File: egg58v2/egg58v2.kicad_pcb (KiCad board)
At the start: 2 copper layers, 141.1 x 125.8 mm, 37 parts, among them J1 AudioJack4, SW11 SW_PUSH_LED, SW12 SW_PUSH_LED, SW13 SW_PUSH_LED, SW14 SW_PUSH_LED, SW15 SW_PUSH_LED, SW16 SW_PUSH_LED, SW21 SW_PUSH_LED, SW22 SW_PUSH_LED, SW23 SW_PUSH_LED, SW24 SW_PUSH_LED, SW25 SW_PUSH_LED, SW26 SW_PUSH_LED, SW31 SW_PUSH_LED, SW32 SW_PUSH_LED, SW33 SW_PUSH_LED, SW34 SW_PUSH_LED, SW35 SW_PUSH_LED, SW36 SW_PUSH_LED, SW41 SW_PUSH_LED, SW42 SW_PUSH_LED, SW43 SW_PUSH_LED, SW44 SW_PUSH_LED, SW45 SW_PUSH_LED, SW46 SW_PUSH_LED, SW52 SW_PUSH_LED, SW53 SW_PUSH_LED, SW54 SW_PUSH_LED, SW55 SW_PUSH_LED, SW56 SW_PUSH_LED, U1 Elite-C

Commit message: columns
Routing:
- net Col6: track 70.7 -> 193.5 mm
- net Col5: track 88.7 -> 204.7 mm
- net Col2: track 140.3 -> 234.0 mm
- net Col3: track 124.5 -> 217.9 mm
- net Col4: track 107.5 -> 200.9 mm
- net Col1: track 162.1 -> 234.3 mm

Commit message: underp footprints and route everything i guess
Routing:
- net GND: track 5.95 -> 224.4 mm, vias 0 -> 57
- net VCC: track 724.2 -> 908.1 mm, vias 6 -> 35
- net Net-(SW46-Pad2): track 0.00 -> 69.0 mm, vias 0 -> 2
- net Col4: track 200.9 -> 249.1 mm, vias 2 -> 7
- net Col5: track 204.7 -> 252.9 mm, vias 2 -> 7
- net Net-(SW55-Pad4): track 0.00 -> 46.6 mm, vias 0 -> 2
- net Col2: track 234.0 -> 280.0 mm, vias 2 -> 7
- net Col3: track 217.9 -> 263.3 mm, vias 2 -> 7
- net Net-(SW54-Pad4): track 0.00 -> 44.6 mm, vias 0 -> 2
- net Net-(SW11-Pad2): track 0.00 -> 43.5 mm, vias 0 -> 3
- net Col6: track 193.5 -> 236.4 mm, vias 0 -> 5
- net Col1: track 234.3 -> 274.7 mm, vias 2 -> 6
- net Net-(SW31-Pad2): track 0.00 -> 39.8 mm, vias 0 -> 2
- net Net-(SW41-Pad2): track 0.00 -> 36.7 mm, vias 0 -> 4
- net Net-(SW26-Pad2): track 0.00 -> 33.4 mm, vias 0 -> 2
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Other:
- board size 141.1 x 125.8 mm -> 141.1 x 127.1 mm

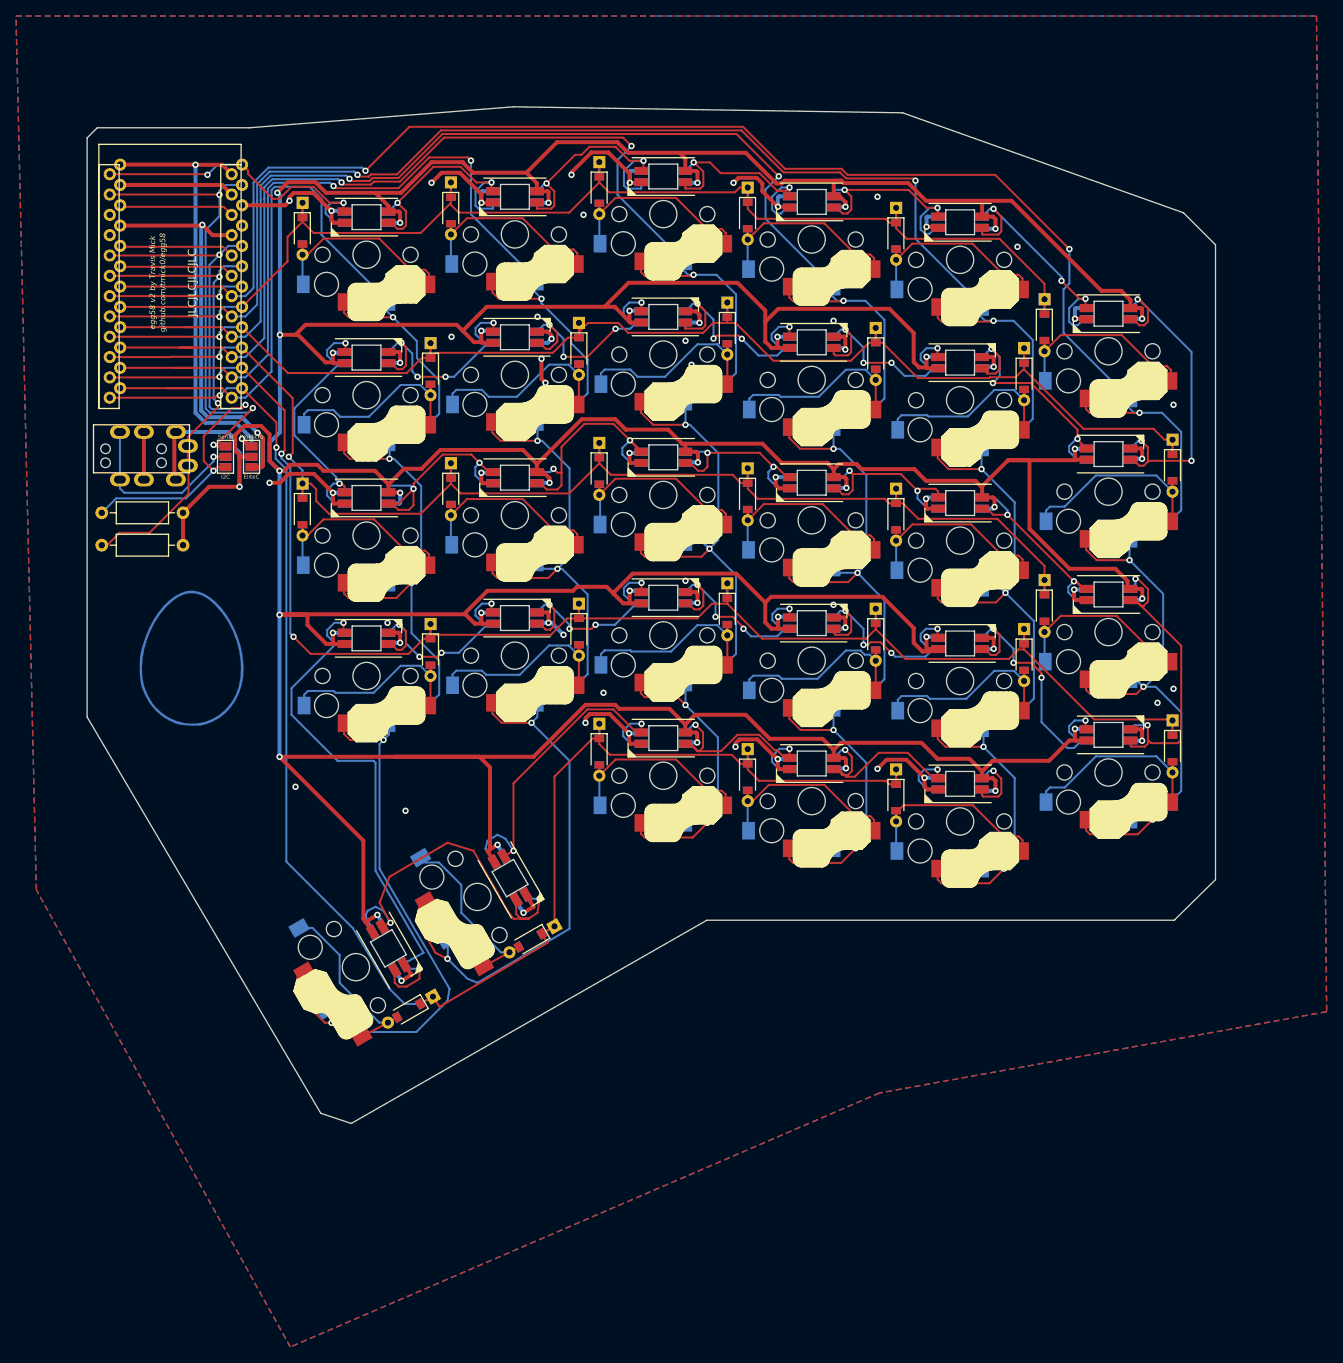
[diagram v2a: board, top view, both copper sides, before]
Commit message: fix (most) vias through silks
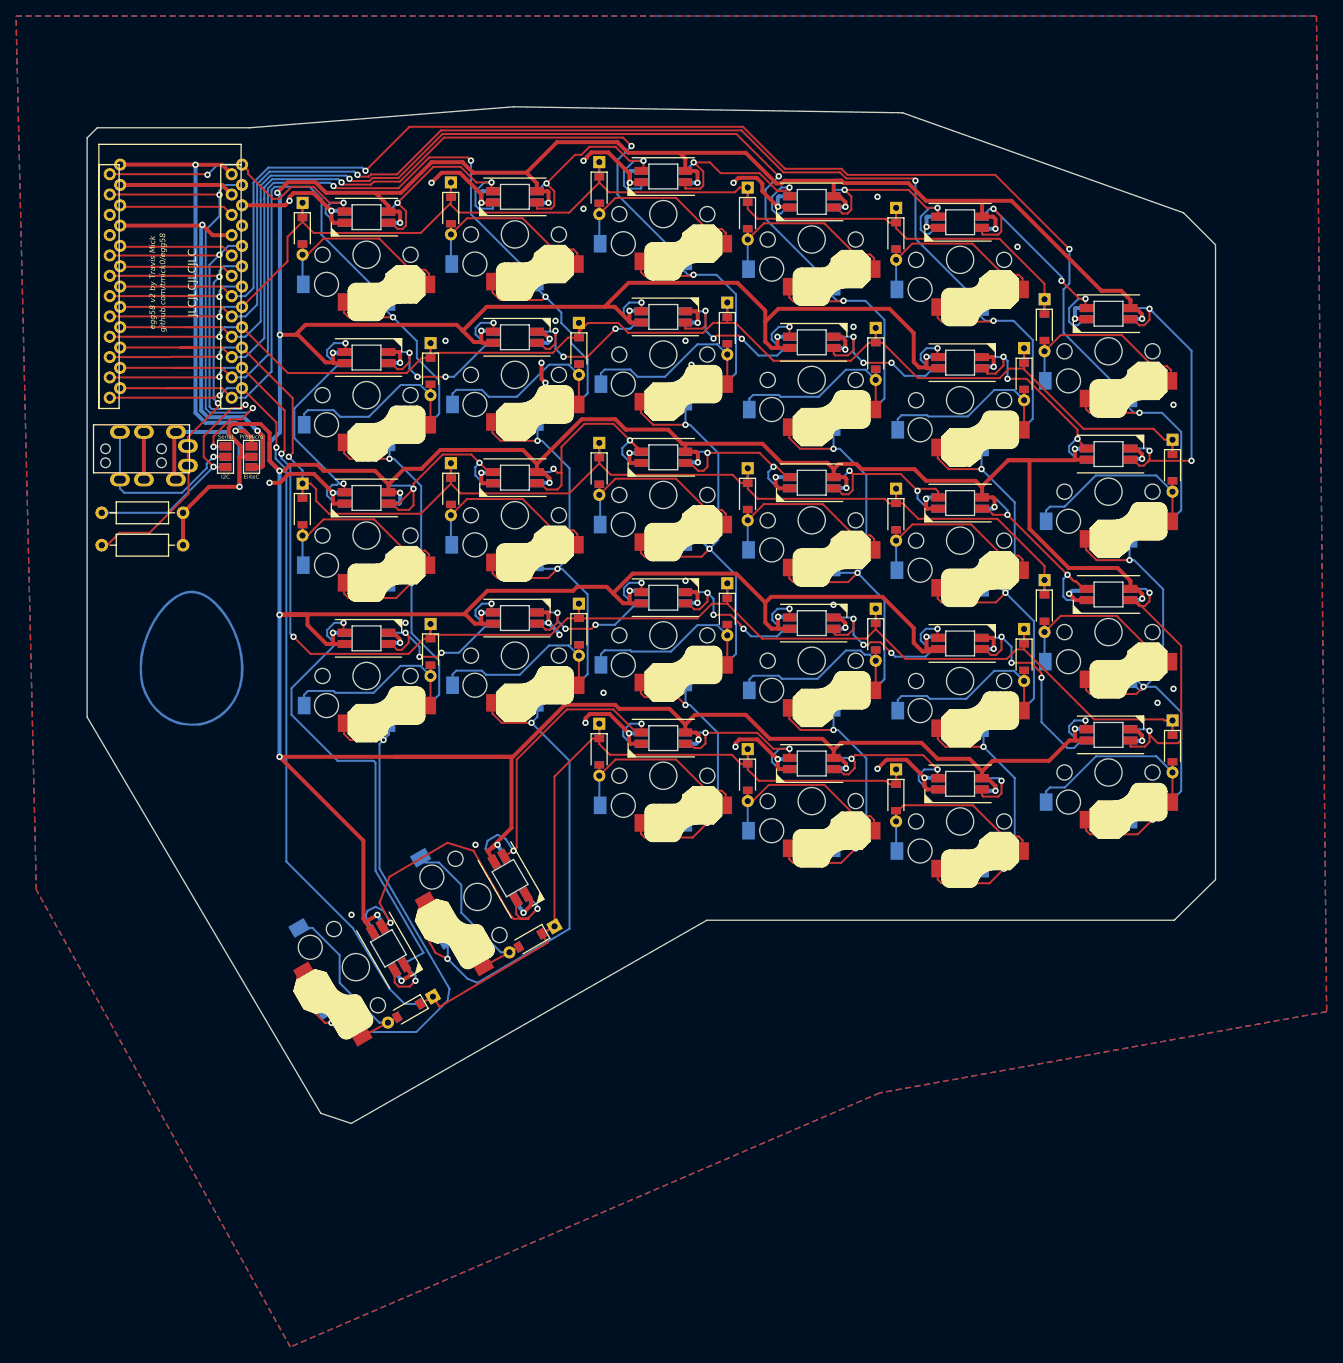
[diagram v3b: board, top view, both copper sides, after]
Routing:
- net GND: track 224.4 -> 218.7 mm
- net VCC: track 908.1 -> 913.4 mm
- net Net-(SW52-Pad4): track 30.3 -> 25.9 mm
- net Net-(SW53-Pad4): track 28.8 -> 24.5 mm
- net Net-(SW21-Pad2): track 32.8 -> 29.0 mm
- net Net-(SW11-Pad2): track 43.5 -> 40.1 mm
- net VBUS: track 57.9 -> 60.5 mm
- net Net-(SW31-Pad4): track 26.7 -> 29.2 mm
- net Net-(SW22-Pad2): track 30.6 -> 28.0 mm
- net Net-(SW25-Pad2): track 30.5 -> 28.1 mm
- net Net-(SW45-Pad2): track 29.4 -> 27.5 mm
- net Net-(SW23-Pad2): track 31.3 -> 29.3 mm
- net Net-(SW41-Pad2): track 36.7 -> 34.8 mm
- net Net-(SW42-Pad2): track 29.7 -> 27.9 mm
- net Net-(SW24-Pad2): track 30.4 -> 28.6 mm
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
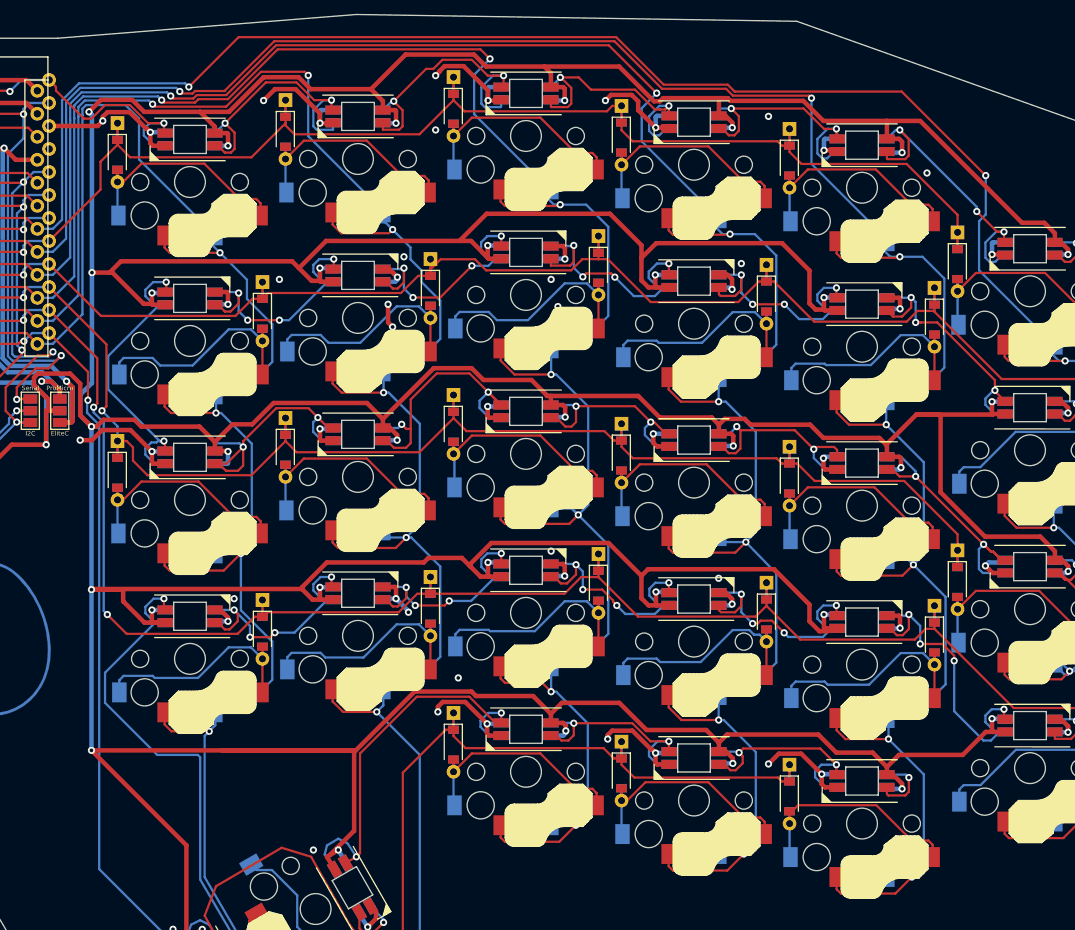
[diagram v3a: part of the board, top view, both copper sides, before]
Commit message: Mounting holes
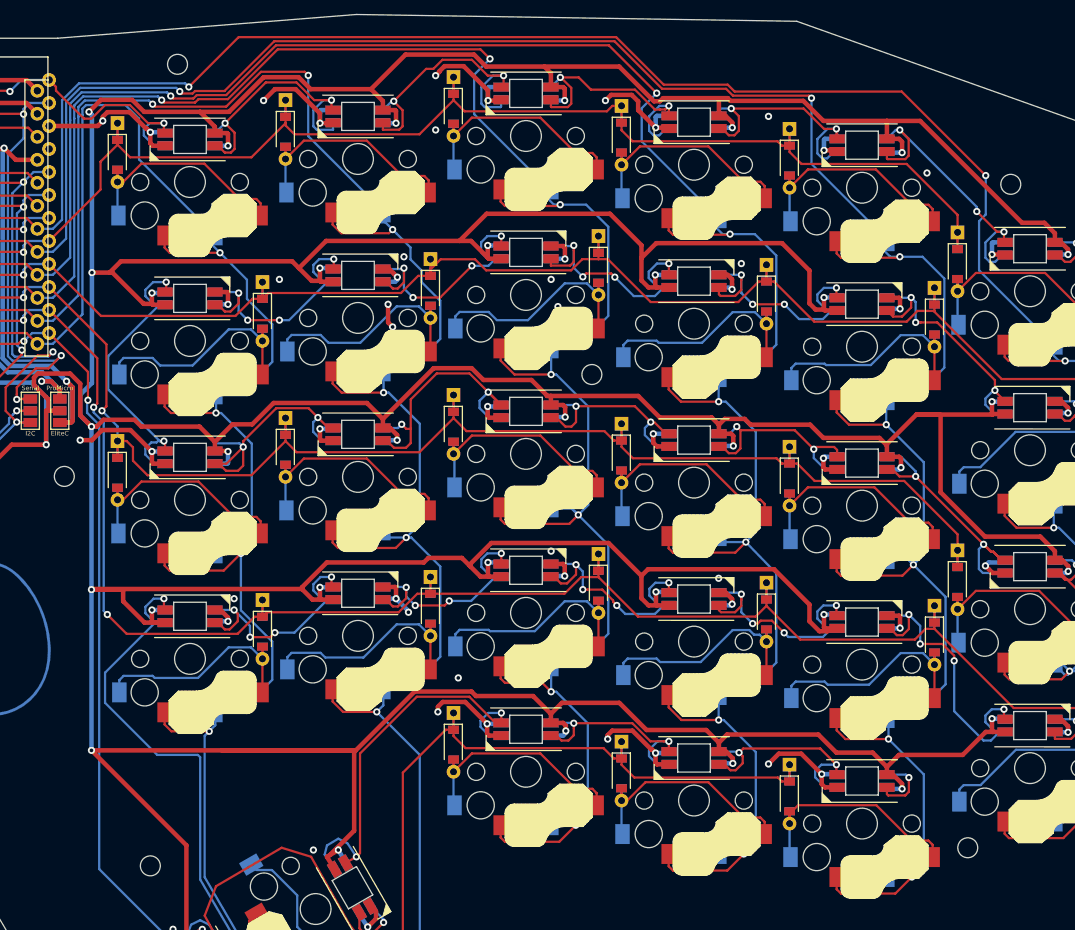
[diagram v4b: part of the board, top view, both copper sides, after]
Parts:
- added REF**: MountingHole_2.2mm_M2, MountingHole:MountingHole_2.2mm_M2, F.Cu at (228.8, 128.8)
- added REF**: MountingHole_2.2mm_M2, MountingHole:MountingHole_2.2mm_M2, F.Cu at (138.5, 130.8)
- added REF**: MountingHole_2.2mm_M2, MountingHole:MountingHole_2.2mm_M2, F.Cu at (141.5, 42.2)
- added REF**: MountingHole_2.2mm_M2, MountingHole:MountingHole_2.2mm_M2, F.Cu at (233.5, 55.5)
- added REF**: MountingHole_2.2mm_M2, MountingHole:MountingHole_2.2mm_M2, F.Cu at (187.2, 76.5)
- added REF**: MountingHole_2.2mm_M2, MountingHole:MountingHole_2.2mm_M2, F.Cu at (129.0, 87.8)
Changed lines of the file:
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@@
     (tracks 2466)
     (zones 0)
-    (modules 37)
+    (modules 43)
     (nets 83)
   )
@@
     (uvia_drill 0.1)
   )
+  (module MountingHole:MountingHole_2.2mm_M2 (layer F.Cu)
+    (at 228.75 128.75)
+    (descr "Mounting Hole 2.2mm, no annular, M2")
+    (tags "mounting hole 2.2mm no annular m2")
+    (attr virtual)
+    (fp_text reference REF** (at 0 -3.2) (layer F.SilkS) hide
+      (effects (font (size 1 1) (thickness 0.15)))
+    )
+    (fp_text value MountingHole_2.2mm_M2 (at 0 3.2) (layer F.Fab)
+      (effects (font (size 1 1) (thickness 0.15)))
+    )
+    (fp_text user %R (at 0.3 0) (layer F.Fab)
+      (effects (font (size 1 1) (thickness 0.15)))
+    )
+    (fp_circle (center 0 0) (end 2.2 0) (layer Cmts.User) (width 0.15))
+    (fp_circle (center 0 0) (end 2.45 0) (layer F.CrtYd) (width 0.05))
+    (pad 1 np_thru_hole circle (at 0 0) (size 2.2 2.2) (drill 2.2) (layers *.Cu *.Mask))
+  )
+  (module MountingHole:MountingHole_2.2mm_M2 (layer F.Cu)
+    (at 138.5 130.75)
+    (descr "Mounting Hole 2.2mm, no annular, M2")
+    (tags "mounting hole 2.2mm no annular m2")
+    (attr virtual)
+    (fp_text reference REF** (at 0 -3.2) (layer F.SilkS) hide
+      (effects (font (size 1 1) (thickness 0.15)))
+    )
+    (fp_text value MountingHole_2.2mm_M2 (at 0 3.2) (layer F.Fab)
+      (effects (font (size 1 1) (thickness 0.15)))
+    )
+    (fp_text user %R (at 0.3 0) (layer F.Fab)
+      (effects (font (size 1 1) (thickness 0.15)))
+    )
+    (fp_circle (center 0 0) (end 2.2 0) (layer Cmts.User) (width 0.15))
+    (fp_circle (center 0 0) (end 2.45 0) (layer F.CrtYd) (width 0.05))
+    (pad 1 np_thru_hole circle (at 0 0) (size 2.2 2.2) (drill 2.2) (layers *.Cu *.Mask))
+  )
+  (module MountingHole:MountingHole_2.2mm_M2 (layer F.Cu)
+    (at 141.5 42.25)
+    (descr "Mounting Hole 2.2mm, no annular, M2")
+    (tags "mounting hole 2.2mm no annular m2")
+    (attr virtual)
+    (fp_text reference REF** (at 0 -3.2) (layer F.SilkS) hide
+      (effects (font (size 1 1) (thickness 0.15)))
+    )
+    (fp_text value MountingHole_2.2mm_M2 (at 0 3.2) (layer F.Fab)
+      (effects (font (size 1 1) (thickness 0.15)))
+    )
+    (fp_text user %R (at 0.3 0) (layer F.Fab)
+      (effects (font (size 1 1) (thickness 0.15)))
+    )
+    (fp_circle (center 0 0) (end 2.2 0) (layer Cmts.User) (width 0.15))
+    (fp_circle (center 0 0) (end 2.45 0) (layer F.CrtYd) (width 0.05))
+    (pad 1 np_thru_hole circle (at 0 0) (size 2.2 2.2) (drill 2.2) (layers *.Cu *.Mask))
+  )
+  (module MountingHole:MountingHole_2.2mm_M2 (layer F.Cu)
+    (at 233.5 55.5)
+    (descr "Mounting Hole 2.2mm, no annular, M2")
+    (tags "mounting hole 2.2mm no annular m2")
+    (attr virtual)
+    (fp_text reference REF** (at 0 -3.2) (layer F.SilkS) hide
+      (effects (font (size 1 1) (thickness 0.15)))
+    )
+    (fp_text value MountingHole_2.2mm_M2 (at 0 3.2) (layer F.Fab)
+      (effects (font (size 1 1) (thickness 0.15)))
+    )
+    (fp_text user %R (at 0.3 0) (layer F.Fab)
+      (effects (font (size 1 1) (thickness 0.15)))
+    )
+    (fp_circle (center 0 0) (end 2.2 0) (layer Cmts.User) (width 0.15))
+    (fp_circle (center 0 0) (end 2.45 0) (layer F.CrtYd) (width 0.05))
+    (pad 1 np_thru_hole circle (at 0 0) (size 2.2 2.2) (drill 2.2) (layers *.Cu *.Mask))
+  )
+  (module MountingHole:MountingHole_2.2mm_M2 (layer F.Cu)
+    (at 187.25 76.5)
+    (descr "Mounting Hole 2.2mm, no annular, M2")
+    (tags "mounting hole 2.2mm no annular m2")
+    (attr virtual)
+    (fp_text reference REF** (at 0 -3.2) (layer F.SilkS) hide
+      (effects (font (size 1 1) (thickness 0.15)))
+    )
+    (fp_text value MountingHole_2.2mm_M2 (at 0 3.2) (layer F.Fab)
+      (effects (font (size 1 1) (thickness 0.15)))
+    )
+    (fp_text user %R (at 0.3 0) (layer F.Fab)
+      (effects (font (size 1 1) (thickness 0.15)))
+    )
+    (fp_circle (center 0 0) (end 2.2 0) (layer Cmts.User) (width 0.15))
+    (fp_circle (center 0 0) (end 2.45 0) (layer F.CrtYd) (width 0.05))
+    (pad 1 np_thru_hole circle (at 0 0) (size 2.2 2.2) (drill 2.2) (layers *.Cu *.Mask))
+  )
+  (module MountingHole:MountingHole_2.2mm_M2 (layer F.Cu)
+    (at 129 87.75)
+    (descr "Mounting Hole 2.2mm, no annular, M2")
+    (tags "mounting hole 2.2mm no annular m2")
+    (attr virtual)
+    (fp_text reference REF** (at 0 -3.2) (layer F.SilkS) hide
+      (effects (font (size 1 1) (thickness 0.15)))
+    )
+    (fp_text value MountingHole_2.2mm_M2 (at 0 3.2) (layer F.Fab)
+      (effects (font (size 1 1) (thickness 0.15)))
+    )
+    (fp_circle (center 0 0) (end 2.45 0) (layer F.CrtYd) (width 0.05))
+    (fp_circle (center 0 0) (end 2.2 0) (layer Cmts.User) (width 0.15))
+    (fp_text user %R (at 0.3 0) (layer F.Fab)
+      (effects (font (size 1 1) (thickness 0.15)))
+    )
+    (pad 1 np_thru_hole circle (at 0 0) (size 2.2 2.2) (drill 2.2) (layers *.Cu *.Mask))
+  )
   (module egg58v2:Choc_Hotswap_SK6812MiniE (layer F.Cu)
